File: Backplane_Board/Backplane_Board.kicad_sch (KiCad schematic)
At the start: 14 parts, among them J1 XT60, J2 XT60, J3 Conn_01x02_Pin, Q1 FDMS86163P, Q2 FDMS86163P, U1 ZXTR2005ZQ-13

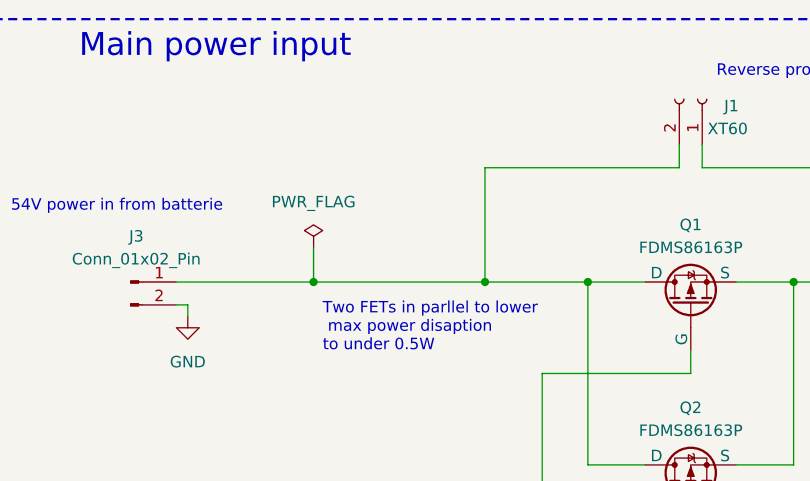
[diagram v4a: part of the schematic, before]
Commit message: got the power input shut layout done ish
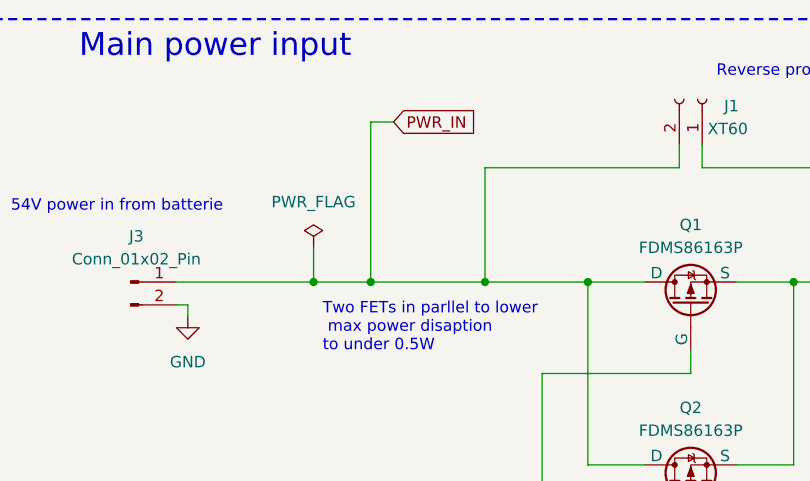
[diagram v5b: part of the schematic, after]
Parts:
- J1, J2: footprint Connector_Wire:SolderWire-2sqmm_1x02_P7.8mm_D2mm_OD3.9mm -> Connector_Wire:SolderWire-0.127sqmm_1x02_P3.7mm_D0.48mm_OD1mm
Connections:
- net PWR_IN: now reaches J1.2 (Pin_2), J3.1 (Pin_1), Q1.1 (D), Q2.1 (D)
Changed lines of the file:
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@@
+	)
+	(junction
+		(at 57.15 41.91)
+		(diameter 0)
+		(color 0 0 0 0)
 	)
 	(junction
@@
 	(wire
 		(pts
+			(xy 57.15 41.91) (xy 69.85 41.91)
+		)
+		(stroke
+			(width 0)
+			(type default)
+		)
+	)
+	(wire
+		(pts
 			(xy 158.75 30.48) (xy 158.75 41.91)
 		)
@@
 	(wire
 		(pts
+			(xy 59.69 24.13) (xy 57.15 24.13)
+		)
+		(stroke
+			(width 0)
+			(type default)
+		)
+	)
+	(wire
+		(pts
 			(xy 35.56 41.91) (xy 50.8 41.91)
 		)
@@
 	(wire
 		(pts
-			(xy 50.8 41.91) (xy 69.85 41.91)
+			(xy 50.8 41.91) (xy 57.15 41.91)
 		)
 		(stroke
@@
 		(pts
 			(xy 109.22 137.16) (xy 90.17 137.16)
+		)
+		(stroke
+			(width 0)
+			(type default)
+		)
+	)
+	(wire
+		(pts
+			(xy 57.15 24.13) (xy 57.15 41.91)
 		)
 		(stroke
@@
 		(property "Intersheetrefs" "${INTERSHEET_REFS}"
 			(at 144.0762 31.75 0)
+			(effects
+				(font
+					(size 1.27 1.27)
+				)
+				(justify left)
+				(hide yes)
+			)
+		)
+	)
+	(global_label "PWR_IN"
+		(shape input)
+		(at 59.69 24.13 0)
+		(fields_autoplaced yes)
+		(effects
+			(font
+				(size 1.27 1.27)
+			)
+			(justify left)
+		)
+		(property "Intersheetrefs" "${INTERSHEET_REFS}"
+			(at 69.5695 24.13 0)
 			(effects
 				(font
@@
 			)
 		)
-		(property "Footprint" "Connector_Wire:SolderWire-2sqmm_1x02_P7.8mm_D2mm_OD3.9mm"
+		(property "Footprint" "Connector_Wire:SolderWire-0.127sqmm_1x02_P3.7mm_D0.48mm_OD1mm"
 			(at 93.98 21.59 0)
 			(effects
@@
 			)
 		)
-		(property "Footprint" "Connector_Wire:SolderWire-2sqmm_1x02_P7.8mm_D2mm_OD3.9mm"
+		(property "Footprint" "Connector_Wire:SolderWire-0.127sqmm_1x02_P3.7mm_D0.48mm_OD1mm"
 			(at 158.75 25.4 0)
 			(effects

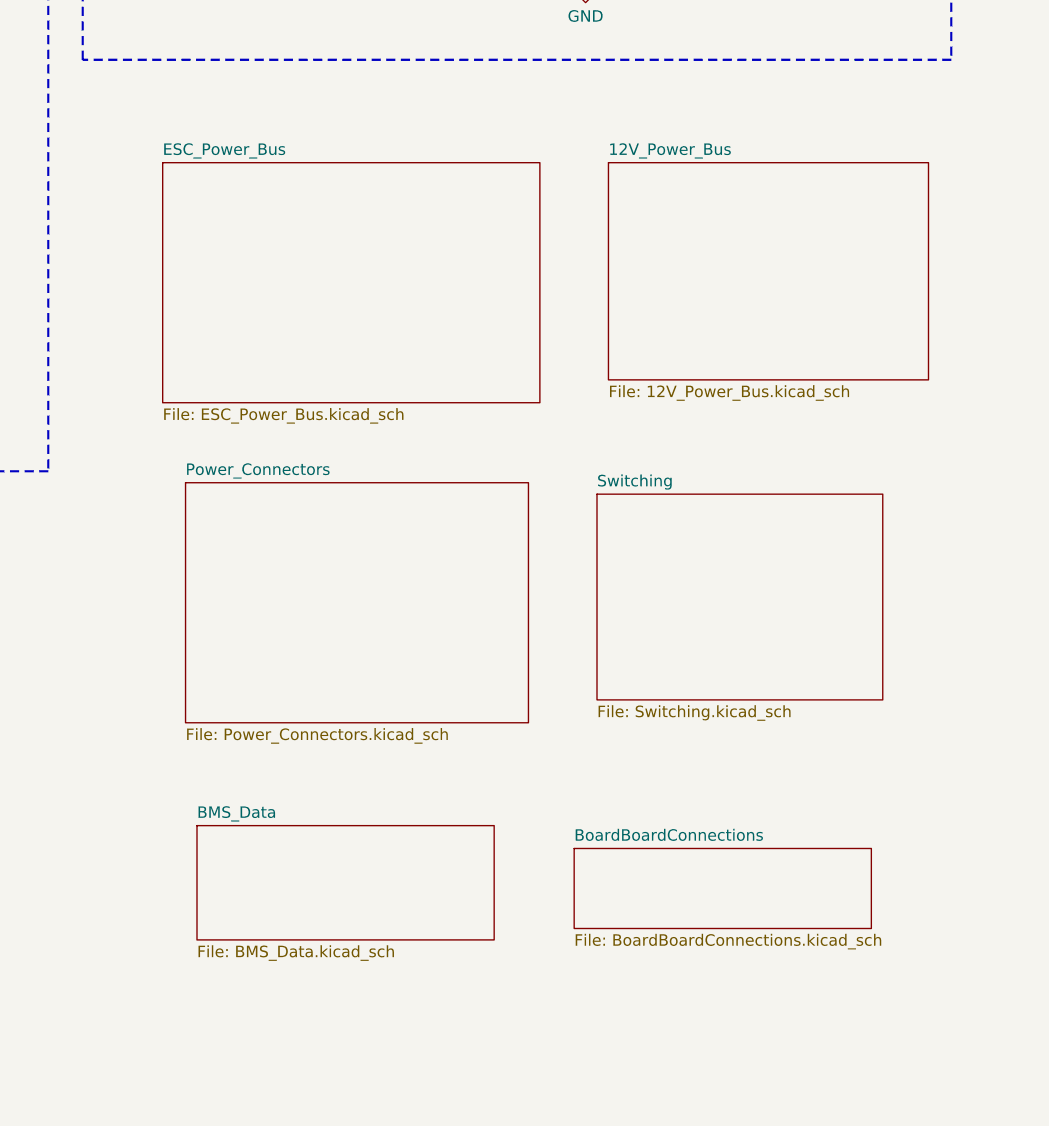
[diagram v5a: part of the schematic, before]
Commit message: added sd card, more drc stuff to fix
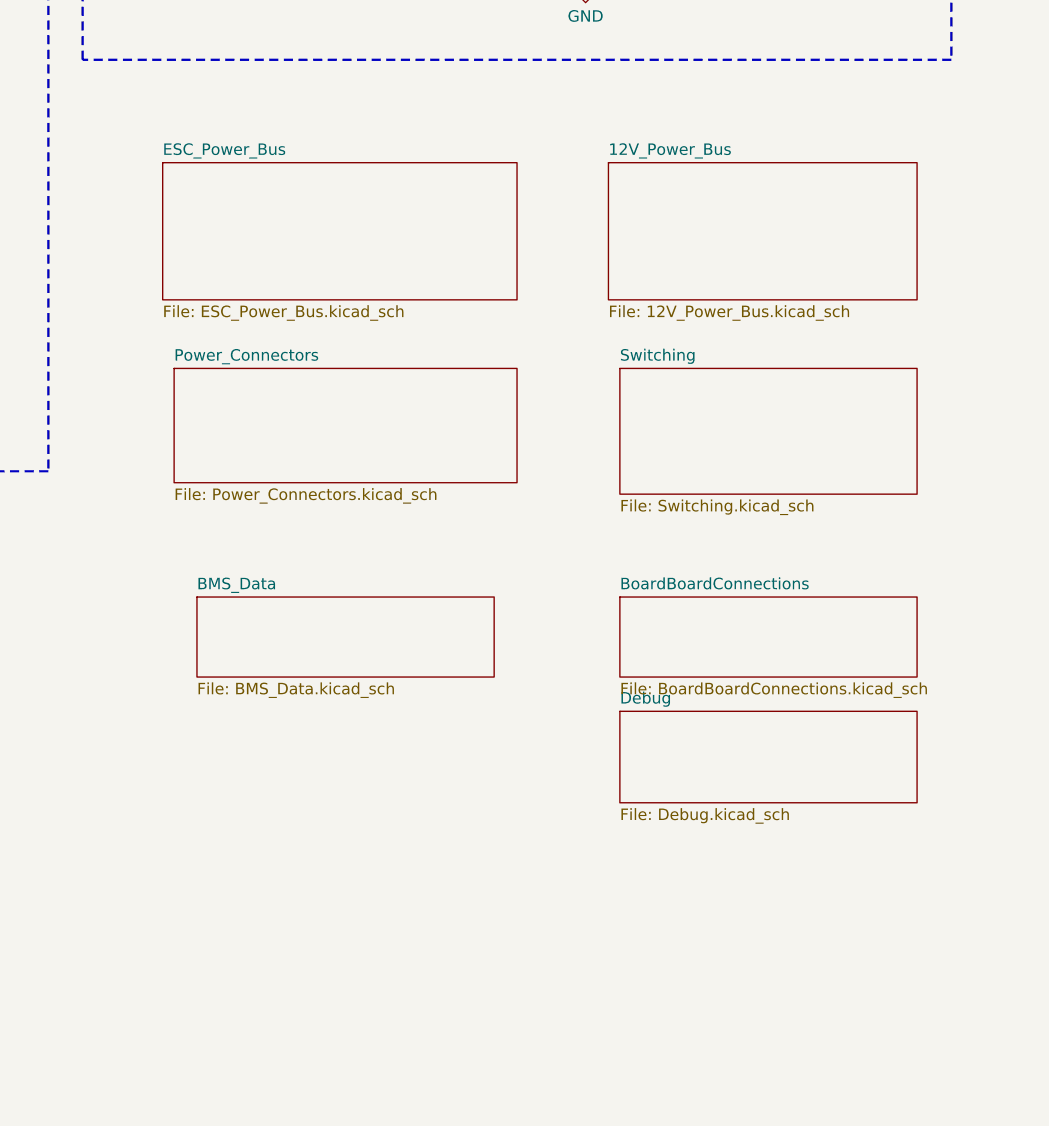
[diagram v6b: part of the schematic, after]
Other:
- added sheet Debug (Debug.kicad_sch)
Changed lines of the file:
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@@
 	)
 	(sheet
-		(at 243.84 109.22)
-		(size 31.75 22.86)
+		(at 246.38 95.25)
+		(size 33.02 13.97)
 		(fields_autoplaced yes)
 		(stroke
@@
 		)
 		(property "Sheetname" "Switching"
-			(at 243.84 108.5084 0)
+			(at 246.38 94.5384 0)
 			(effects
 				(font
@@
 		)
 		(property "Sheetfile" "Switching.kicad_sch"
-			(at 243.84 132.6646 0)
+			(at 246.38 109.8046 0)
 			(effects
 				(font
@@
 	)
 	(sheet
-		(at 198.12 107.95)
-		(size 38.1 26.67)
+		(at 246.38 133.35)
+		(size 33.02 10.16)
+		(fields_autoplaced yes)
+		(stroke
+			(width 0.1524)
+			(type solid)
+		)
+		(fill
+			(color 0 0 0 0.0000)
+		)
+		(property "Sheetname" "Debug"
+			(at 246.38 132.6384 0)
+			(effects
+				(font
+					(size 1.27 1.27)
+				)
+				(justify left bottom)
+			)
+		)
+		(property "Sheetfile" "Debug.kicad_sch"
+			(at 246.38 144.0946 0)
+			(effects
+				(font
+					(size 1.27 1.27)
+				)
+				(justify left top)
+			)
+		)
+		(instances
+			(project "Backplane_Board"
+				(path "/4484cfee-9e43-4cef-88b4-a8ca308542b4"
+					(page "8")
+				)
+			)
+		)
+	)
+	(sheet
+		(at 196.85 95.25)
+		(size 38.1 12.7)
 		(fields_autoplaced yes)
 		(stroke
@@
 		)
 		(property "Sheetname" "Power_Connectors"
-			(at 198.12 107.2384 0)
+			(at 196.85 94.5384 0)
 			(effects
 				(font
@@
 		)
 		(property "Sheetfile" "Power_Connectors.kicad_sch"
-			(at 198.12 135.2046 0)
+			(at 196.85 108.5346 0)
 			(effects
 				(font
@@
 	(sheet
 		(at 245.11 72.39)
-		(size 35.56 24.13)
+		(size 34.29 15.24)
 		(fields_autoplaced yes)
 		(stroke
@@
 		)
 		(property "Sheetfile" "12V_Power_Bus.kicad_sch"
-			(at 245.11 97.1046 0)
+			(at 245.11 88.2146 0)
 			(effects
 				(font
@@
 	)
 	(sheet
-		(at 199.39 146.05)
-		(size 33.02 12.7)
+		(at 199.39 120.65)
+		(size 33.02 8.89)
 		(fields_autoplaced yes)
 		(stroke
@@
 		)
 		(property "Sheetname" "BMS_Data"
-			(at 199.39 145.3384 0)
+			(at 199.39 119.9384 0)
 			(effects
 				(font
@@
 		)
 		(property "Sheetfile" "BMS_Data.kicad_sch"
-			(at 199.39 159.3346 0)
+			(at 199.39 130.1246 0)
 			(effects
 				(font
@@
 	)
 	(sheet
-		(at 241.3 148.59)
+		(at 246.38 120.65)
 		(size 33.02 8.89)
 		(fields_autoplaced yes)
@@
 		)
 		(property "Sheetname" "BoardBoardConnections"
-			(at 241.3 147.8784 0)
+			(at 246.38 119.9384 0)
 			(effects
 				(font
@@
 		)
 		(property "Sheetfile" "BoardBoardConnections.kicad_sch"
-			(at 241.3 158.0646 0)
+			(at 246.38 130.1246 0)
 			(effects
 				(font
@@
 	(sheet
 		(at 195.58 72.39)
-		(size 41.91 26.67)
+		(size 39.37 15.24)
 		(fields_autoplaced yes)
 		(stroke
@@
 		)
 		(property "Sheetfile" "ESC_Power_Bus.kicad_sch"
-			(at 195.58 99.6446 0)
-			(effects
-				(font
+			(at 195.58 88.2146 0)
+			(effects
+				(font

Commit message: clean up
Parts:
- added TP5: TestPoint, TestPoint:TestPoint_Pad_2.5x2.5mm, symbol Connector:TestPoint
- J1, J2: now not fitted; now left out of the parts list
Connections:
- net at D1.2 (A), Q1.2 (G), Q2.2 (G)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: now also TP5.1
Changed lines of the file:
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@@
+	)
+	(junction
+		(at 76.2 63.5)
+		(diameter 0)
+		(color 0 0 0 0)
 	)
 	(junction
@@
 	(wire
 		(pts
+			(xy 76.2 63.5) (xy 76.2 73.66)
+		)
+		(stroke
+			(width 0)
+			(type default)
+		)
+	)
+	(wire
+		(pts
 			(xy 92.71 76.2) (xy 92.71 81.28)
 		)
@@
 	(wire
 		(pts
+			(xy 59.69 63.5) (xy 76.2 63.5)
+		)
+		(stroke
+			(width 0)
+			(type default)
+		)
+	)
+	(wire
+		(pts
 			(xy 91.44 26.67) (xy 91.44 29.21)
 		)
@@
 	(wire
 		(pts
-			(xy 76.2 52.07) (xy 76.2 73.66)
+			(xy 76.2 52.07) (xy 76.2 63.5)
 		)
 		(stroke
@@
 		(pts
 			(xy 97.79 41.91) (xy 104.14 41.91)
+		)
+		(stroke
+			(width 0)
+			(type default)
+		)
+	)
+	(wire
+		(pts
+			(xy 59.69 68.58) (xy 59.69 63.5)
 		)
 		(stroke
@@
 	)
 	(symbol
+		(lib_id "Connector:TestPoint")
+		(at 59.69 68.58 180)
+		(unit 1)
+		(exclude_from_sim no)
+		(in_bom yes)
+		(on_board yes)
+		(dnp no)
+		(fields_autoplaced yes)
+		(property "Reference" "TP5"
+			(at 62.23 70.6119 0)
+			(effects
+				(font
+					(size 1.27 1.27)
+				)
+				(justify right)
+			)
+		)
+		(property "Value" "TestPoint"
+			(at 62.23 73.1519 0)
+			(effects
+				(font
+					(size 1.27 1.27)
+				)
+				(justify right)
+			)
+		)
+		(property "Footprint" "TestPoint:TestPoint_Pad_2.5x2.5mm"
+			(at 54.61 68.58 0)
+			(effects
+				(font
+					(size 1.27 1.27)
+				)
+				(hide yes)
+			)
+		)
+		(property "Datasheet" "~"
+			(at 54.61 68.58 0)
+			(effects
+				(font
+					(size 1.27 1.27)
+				)
+				(hide yes)
+			)
+		)
+		(property "Description" "test point"
+			(at 59.69 68.58 0)
+			(effects
+				(font
+					(size 1.27 1.27)
+				)
+				(hide yes)
+			)
+		)
+		(pin "1"
+		)
+		(instances
+			(project "Backplane_Board"
+				(path "/4484cfee-9e43-4cef-88b4-a8ca308542b4"
+					(reference "TP5")
+					(unit 1)
+				)
+			)
+		)
+	)
+	(symbol
 		(lib_id "Connector:Conn_01x02_Pin")
 		(at 30.48 41.91 0)
@@
 		(mirror x)
 		(unit 1)
-		(exclude_from_sim no)
-		(in_bom yes)
-		(on_board yes)
-		(dnp no)
+		(exclude_from_sim yes)
+		(in_bom no)
+		(on_board no)
+		(dnp yes)
 		(property "Reference" "J1"
 			(at 98.044 22.352 90)
@@
 		(mirror x)
 		(unit 1)
-		(exclude_from_sim no)
-		(in_bom yes)
-		(on_board yes)
-		(dnp no)
+		(exclude_from_sim yes)
+		(in_bom no)
+		(on_board no)
+		(dnp yes)
 		(property "Reference" "J2"
 			(at 162.814 26.162 90)

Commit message: add anotations
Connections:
- net GND: now also J3.1 (Pin_1); no longer J3.2 (Pin_2)
- net PWR_IN: now also J3.2 (Pin_2); no longer J3.1 (Pin_1)
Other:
- moved on the sheet: J3
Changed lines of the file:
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@@
+	)
+	(junction
+		(at 50.8 41.91)
+		(diameter 0)
+		(color 0 0 0 0)
 	)
 	(junction
@@
 	)
 	(junction
-		(at 50.8 41.91)
-		(diameter 0)
-		(color 0 0 0 0)
-	)
-	(junction
 		(at 242.57 48.26)
 		(diameter 0)
@@
 	(wire
 		(pts
-			(xy 36.83 44.45) (xy 35.56 44.45)
-		)
-		(stroke
-			(width 0)
-			(type default)
-		)
-	)
-	(wire
-		(pts
 			(xy 115.57 59.69) (xy 115.57 76.2)
 		)
@@
 	(wire
 		(pts
+			(xy 33.02 44.45) (xy 39.37 44.45)
+		)
+		(stroke
+			(width 0)
+			(type default)
+		)
+	)
+	(wire
+		(pts
 			(xy 76.2 73.66) (xy 92.71 73.66)
 		)
@@
 	(wire
 		(pts
-			(xy 35.56 41.91) (xy 50.8 41.91)
-		)
-		(stroke
-			(width 0)
-			(type default)
-		)
-	)
-	(wire
-		(pts
 			(xy 130.81 41.91) (xy 156.21 41.91)
 		)
@@
 	(wire
 		(pts
-			(xy 36.83 45.72) (xy 36.83 44.45)
+			(xy 39.37 48.26) (xy 39.37 44.45)
 		)
 		(stroke
@@
 		(pts
 			(xy 50.8 137.16) (xy 74.93 137.16)
+		)
+		(stroke
+			(width 0)
+			(type default)
+		)
+	)
+	(wire
+		(pts
+			(xy 33.02 41.91) (xy 50.8 41.91)
 		)
 		(stroke
@@
 	(symbol
 		(lib_id "Connector:Conn_01x02_Pin")
-		(at 30.48 41.91 0)
+		(at 27.94 44.45 0)
+		(mirror x)
 		(unit 1)
 		(exclude_from_sim no)
@@
 		(on_board yes)
 		(dnp no)
-		(fields_autoplaced yes)
 		(property "Reference" "J3"
-			(at 31.115 36.83 0)
+			(at 28.575 49.53 0)
 			(effects
 				(font
@@
 		)
 		(property "Value" "Conn_01x02_Pin"
-			(at 31.115 39.37 0)
+			(at 28.575 46.99 0)
 			(effects
 				(font
@@
 		)
 		(property "Footprint" "Connector_AMASS:AMASS_XT60-M_1x02_P7.20mm_Vertical"
-			(at 30.48 41.91 0)
+			(at 27.94 44.45 0)
 			(effects
 				(font
@@
 		)
 		(property "Datasheet" "~"
-			(at 30.48 41.91 0)
+			(at 27.94 44.45 0)
 			(effects
 				(font
@@
 		)
 		(property "Description" "Generic connector, single row, 01x02, script generated"
-			(at 30.48 41.91 0)
+			(at 27.94 44.45 0)
 			(effects
 				(font
@@
 	(symbol
 		(lib_id "power:GND")
-		(at 36.83 45.72 0)
+		(at 39.37 48.26 0)
 		(unit 1)
 		(exclude_from_sim no)
@@
 		(fields_autoplaced yes)
 		(property "Reference" "#PWR01"
-			(at 36.83 52.07 0)
+			(at 39.37 54.61 0)
 			(effects
 				(font
@@
 		)
 		(property "Value" "GND"
-			(at 36.83 50.8 0)
+			(at 39.37 53.34 0)
 			(effects
 				(font
@@
 		)
 		(property "Footprint" ""
-			(at 36.83 45.72 0)
+			(at 39.37 48.26 0)
 			(effects
 				(font
@@
 		)
 		(property "Datasheet" ""
-			(at 36.83 45.72 0)
+			(at 39.37 48.26 0)
 			(effects
 				(font
@@
 		)
 		(property "Description" "Power symbol creates a global label with name \"GND\" , ground"
-			(at 36.83 45.72 0)
+			(at 39.37 48.26 0)
 			(effects
 				(font
@@
 	)
 	(sheet
-		(at 246.38 133.35)
+		(at 246.38 134.62)
 		(size 33.02 10.16)
 		(fields_autoplaced yes)
@@
 		)
 		(property "Sheetname" "Debug"
-			(at 246.38 132.6384 0)
+			(at 246.38 133.9084 0)
 			(effects
 				(font
@@
 		)
 		(property "Sheetfile" "Debug.kicad_sch"
-			(at 246.38 144.0946 0)
-			(effects
-				(font
+			(at 246.38 145.3646 0)
+			(effects
+				(font
